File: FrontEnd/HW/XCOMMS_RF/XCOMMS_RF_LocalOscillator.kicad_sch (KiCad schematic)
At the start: 28 parts, among them U4 LMX2572RHAT, Y1 TCXO 25 MHz

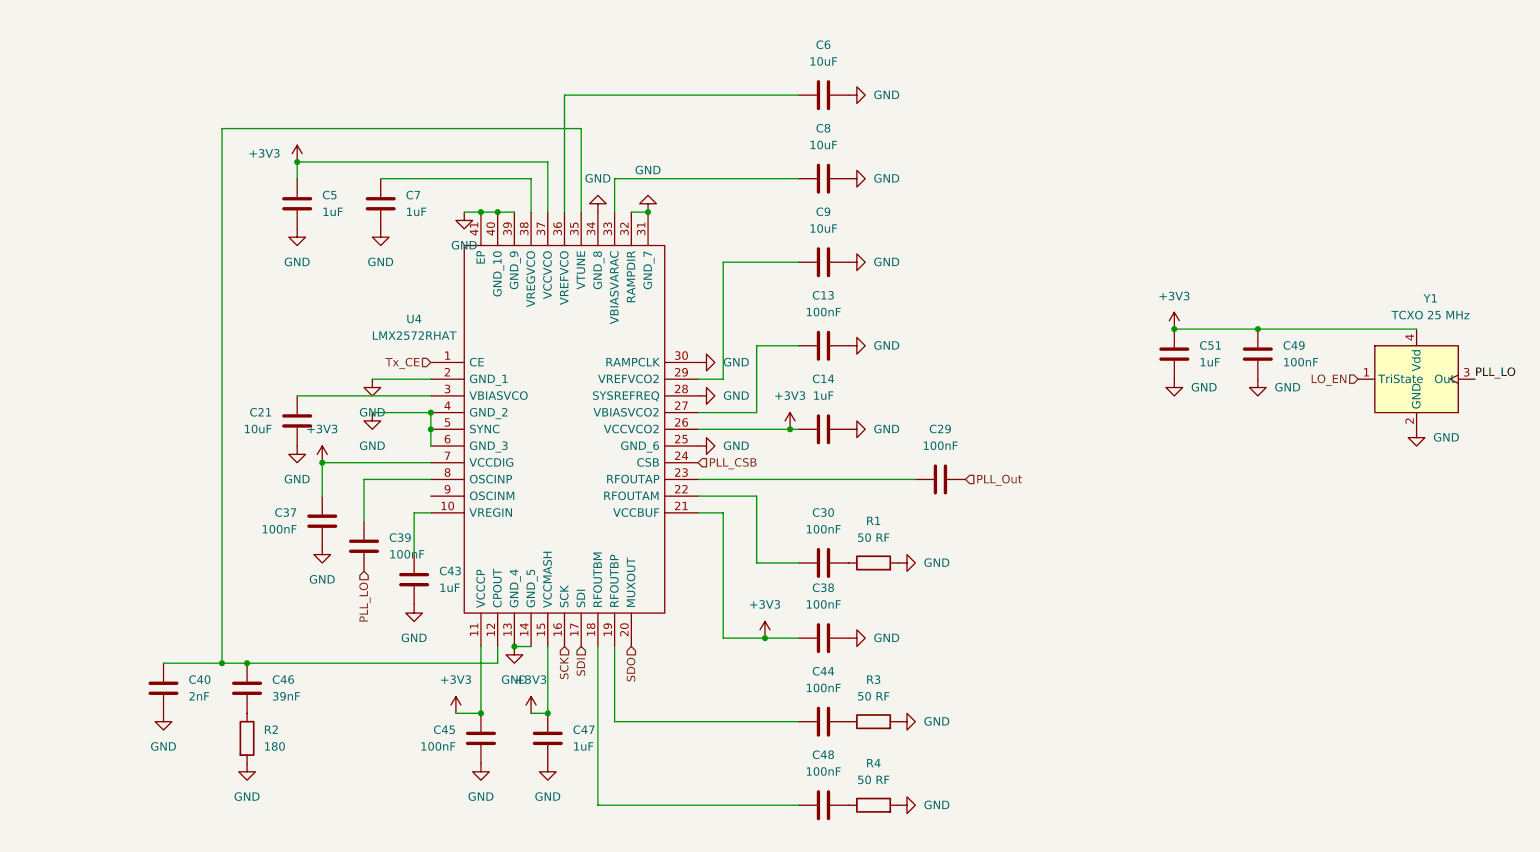
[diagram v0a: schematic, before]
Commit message: XCOMMS_RF ported to KiCad
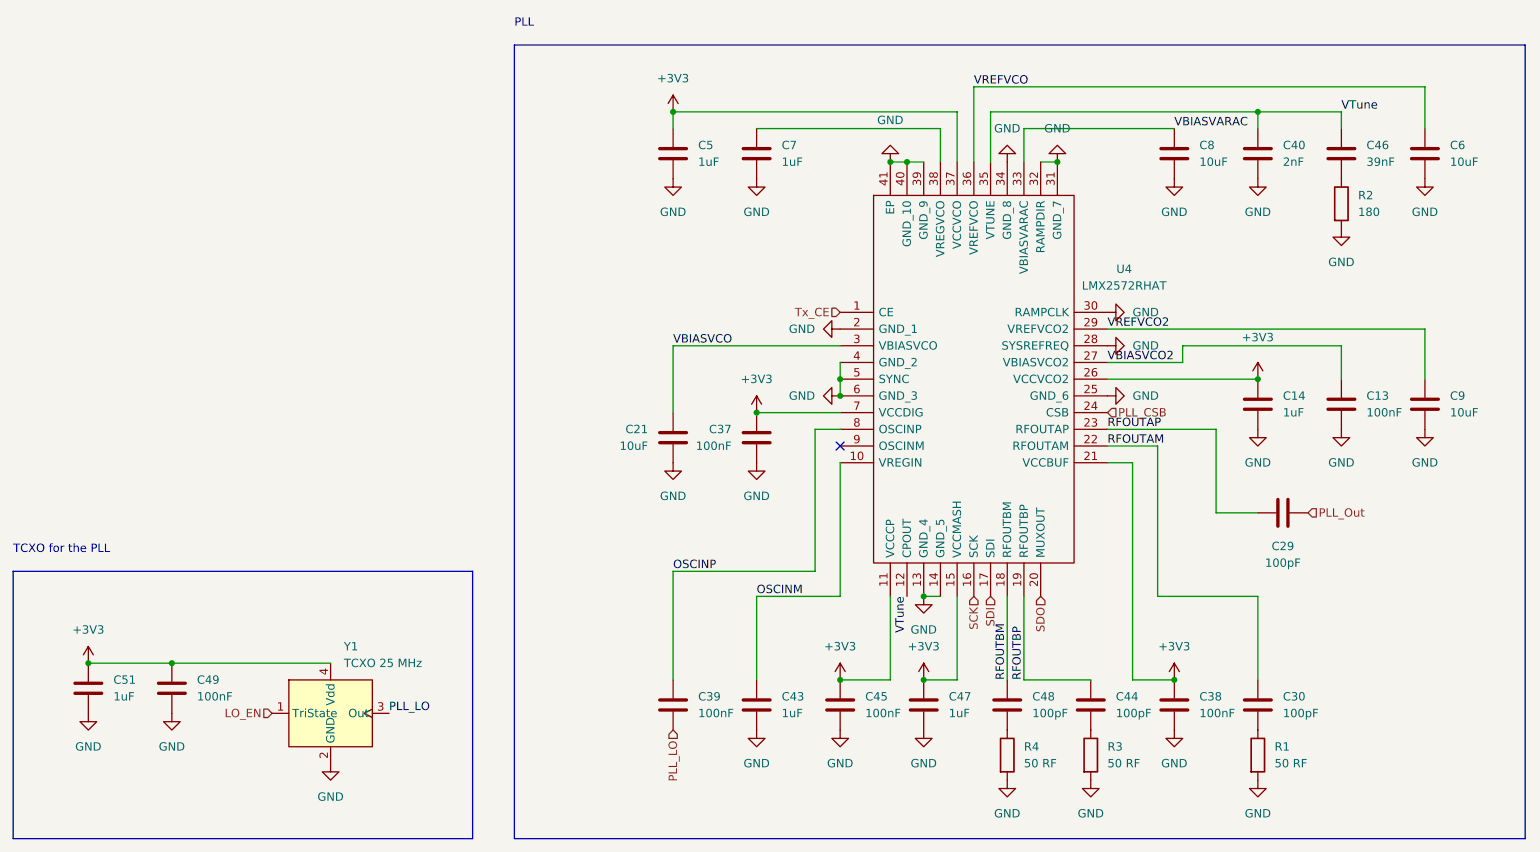
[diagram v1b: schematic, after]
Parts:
- C29, C30, C44, C48: value 100nF -> 100pF; footprint Capacitor_SMD:C_0603_1608Metric -> Capacitor_SMD:C_0402_1005Metric
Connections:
- net PLL_Out: now also C29.2; no longer C29.1
- net RFOUTAP: now reaches U4.23 (RFOUTAP)
- net RFOUTAP: now also C29.1; no longer C29.2
- net VBIASVCO: now reaches C21.2, U4.3 (VBIASVCO)
- net RFOUTAM: now reaches C30.2, U4.22 (RFOUTAM)
- net RFOUTBP: now reaches C44.2, U4.19 (RFOUTBP)
- net OSCINM: now reaches C43.2, U4.10 (VREGIN)
- net VTune: now reaches C40.2, C46.2, U4.12 (CPOUT), U4.35 (VTUNE)
- net RFOUTBM: now reaches C48.2, U4.18 (RFOUTBM)
- net VBIASVCO2: now reaches C13.2, U4.27 (VBIASVCO2)
- net VREFVCO2: now reaches C9.2, U4.29 (VREFVCO2)
- net VBIASVARAC: now reaches C8.2, U4.33 (VBIASVARAC)
- net VREFVCO: now reaches C6.2, U4.36 (VREFVCO)
- net OSCINP: now reaches C39.2, U4.8 (OSCINP)
- no-connect marks 0 -> 1
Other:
- note added: "PLL"
- note added: "TCXO for the PLL"
- moved on the sheet: C13, C14, C21, C37, C38, C39, C40, C43, C45, C46, C47, C49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

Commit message: XCOMS_RF updated
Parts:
- C21: value 10uF -> 470nF
- C7: value 1uF -> 10nF
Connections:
- net VREGVCO: now reaches C7.2, U4.38 (VREGVCO)
- net Tx_CE renamed PLL_CE
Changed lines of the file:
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@@
     (stroke (width 0) (type default) (color 0 0 0 0))
   )
-  (wire (pts (xy 217.17 78.74) (xy 217.17 81.28))
-    (stroke (width 0) (type default) (color 0 0 0 0))
-  )
-  (wire (pts (xy 241.3 78.74) (xy 241.3 83.82))
+  (wire (pts (xy 217.17 80.01) (xy 217.17 81.28))
+    (stroke (width 0) (type default) (color 0 0 0 0))
+  )
+  (wire (pts (xy 241.3 80.01) (xy 241.3 83.82))
     (stroke (width 0) (type default) (color 0 0 0 0))
   )
@@
     (stroke (width 0) (type default) (color 0 0 0 0))
   )
-  (wire (pts (xy 217.17 78.74) (xy 241.3 78.74))
+  (wire (pts (xy 217.17 80.01) (xy 241.3 80.01))
     (stroke (width 0) (type default) (color 0 0 0 0))
   )
@@
   )
   (label "VREFVCO2" (at 205.74 76.2 0)
+    (effects (font (size 1.27 1.27)) (justify left bottom))
+  )
+  (label "VREGVCO" (at 152.4 45.72 0)
     (effects (font (size 1.27 1.27)) (justify left bottom))
   )
@@
     (effects (font (size 1.27 1.27)) (justify left bottom))
   )
-  (hierarchical_label "Tx_CE" (shape input) (at 165.1 73.66 180)
+  (hierarchical_label "PLL_CE" (shape input) (at 165.1 73.66 180)
     (effects (font (size 1.27 1.27)) (justify right))
   )
@@
       (effects (font (size 1.27 1.27)) (justify right))
     )
-    (property "Value" "10uF" (id 1) (at 135.89 93.9799 0)
+    (property "Value" "470nF" (id 1) (at 135.89 93.9799 0)
       (effects (font (size 1.27 1.27)) (justify right))
     )
@@
       (effects (font (size 1.27 1.27)) (justify right))
     )
-    (property "Value" "1uF" (id 1) (at 156.21 50.7999 0)
+    (property "Value" "10nF" (id 1) (at 156.21 50.7999 0)
       (effects (font (size 1.27 1.27)) (justify right))
     )
@@
   )
   (symbol (lib_id "power:+3V3") (at 228.6 83.82 0) (unit 1)
-    (in_bom yes) (on_board yes) (fields_autoplaced)
+    (in_bom yes) (on_board yes)
     (property "Reference" "#PWR0157" (id 0) (at 228.6 87.63 0)
       (effects (font (size 1.27 1.27)) hide)
     )
-    (property "Value" "+3V3" (id 1) (at 228.6 77.47 0))
+    (property "Value" "+3V3" (id 1) (at 232.41 81.28 0))
     (property "Footprint" "" (id 2) (at 228.6 83.82 0)
       (effects (font (size 1.27 1.27)) hide)

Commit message: XCOMMS RF Update
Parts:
- C21, C6, C8, C9: footprint Capacitor_SMD:C_0805_2012Metric -> Capacitor_SMD:C_0603_1608Metric
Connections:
- net LO_EN is gone; now on net PLL_CE: Y1.1 (TriState)
- net OSCINM renamed VREGIN
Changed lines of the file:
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@@
     (effects (font (size 1.27 1.27)) (justify left bottom))
   )
-  (label "OSCINM" (at 152.4 116.84 0)
+  (label "VREGIN" (at 152.4 116.84 0)
     (effects (font (size 1.27 1.27)) (justify left bottom))
   )
@@
     (effects (font (size 1.27 1.27)) (justify left))
   )
-  (hierarchical_label "LO_EN" (shape input) (at 78.74 134.62 180)
-    (effects (font (size 1.27 1.27)) (justify right))
-  )
   (hierarchical_label "SDI" (shape input) (at 187.96 116.84 270)
     (effects (font (size 1.27 1.27)) (justify right))
@@
     (effects (font (size 1.27 1.27)) (justify right))
   )
+  (hierarchical_label "PLL_CE" (shape input) (at 78.74 134.62 180)
+    (effects (font (size 1.27 1.27)) (justify right))
+  )
   (hierarchical_label "SCK" (shape input) (at 185.42 116.84 270)
     (effects (font (size 1.27 1.27)) (justify right))
@@
       (effects (font (size 1.27 1.27)) (justify right))
     )
-    (property "Footprint" "Capacitor_SMD:C_0805_2012Metric" (id 2) (at 140.6652 88.9 0)
+    (property "Footprint" "Capacitor_SMD:C_0603_1608Metric" (id 2) (at 140.6652 88.9 0)
       (effects (font (size 1.27 1.27)) hide)
     )
@@
       (effects (font (size 1.27 1.27)) (justify right))
     )
-    (property "Footprint" "Capacitor_SMD:C_0805_2012Metric" (id 2) (at 253.0348 45.72 0)
+    (property "Footprint" "Capacitor_SMD:C_0603_1608Metric" (id 2) (at 253.0348 45.72 0)
       (effects (font (size 1.27 1.27)) hide)
     )
@@
       (effects (font (size 1.27 1.27)) (justify right))
     )
-    (property "Footprint" "Capacitor_SMD:C_0805_2012Metric" (id 2) (at 214.9348 45.72 0)
+    (property "Footprint" "Capacitor_SMD:C_0603_1608Metric" (id 2) (at 214.9348 45.72 0)
       (effects (font (size 1.27 1.27)) hide)
     )
@@
       (effects (font (size 1.27 1.27)) (justify right))
     )
-    (property "Footprint" "Capacitor_SMD:C_0805_2012Metric" (id 2) (at 253.0348 83.82 0)
-      (effects (font (size 1.27 1.27)) hide)
-    )
+    (property "Footprint" "Capacitor_SMD:C_0603_1608Metric" (id 2) (at 253.0348 83.82 0)
+      (effects (font (size 1.27 1.27)) hide)
+    )

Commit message: XCOMMS RF
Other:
- moved on the sheet: C13, C14, C21, C29, C30, C37, C38, C39, C40, C43, C44, C45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
